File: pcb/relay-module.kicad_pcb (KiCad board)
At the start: 4 copper layers, 50 x 50 mm, 92 parts, among them J1 AVR-UPDI-6, J2 QWICC, J3 Power In, J4 Power Out, K1 PR24-5V-900-1A, P1 MountingHole_Pad, P2 MountingHole_Pad, P3 MountingHole_Pad, P4 MountingHole_Pad, Q1 MMBT3904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

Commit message: schematic and PCB clean up
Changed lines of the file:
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@@
 				(font
 					(size 0.001 0.001)
+					(thickness 0.15)
 				)
 			)
@@
 				(font
 					(size 0.001 0.001)
+					(thickness 0.15)
 				)
 			)
@@
 				(font
 					(size 0.001 0.001)
+					(thickness 0.15)
 				)
 				(justify mirror)
@@
 				(font
 					(size 0.001 0.001)
+					(thickness 0.15)
 				)
 				(justify mirror)
@@
 				(font
 					(size 0.001 0.001)
+					(thickness 0.15)
 				)
 				(justify mirror)
@@
 				(font
 					(size 0.001 0.001)
+					(thickness 0.15)
 				)
 				(justify mirror)
@@
 				(font
 					(size 0.001 0.001)
+					(thickness 0.15)
 				)
 				(justify mirror)
@@
 				(font
 					(size 0.001 0.001)
+					(thickness 0.15)
 				)
 				(justify mirror)
@@
 				(font
 					(size 0.001 0.001)
+					(thickness 0.15)
 				)
 				(justify mirror)
@@
 				(font
 					(size 0.001 0.001)
+					(thickness 0.15)
 				)
 				(justify mirror)
@@
 				(font
 					(size 0.001 0.001)
+					(thickness 0.15)
 				)
 				(justify mirror)
@@
 				(font
 					(size 0.001 0.001)
+					(thickness 0.15)
 				)
 				(justify mirror)
@@
 				(font
 					(size 0.001 0.001)
+					(thickness 0.15)
 				)
 				(justify mirror)
@@
 				(font
 					(size 0.001 0.001)
+					(thickness 0.15)
 				)
 				(justify mirror)
@@
 				(font
 					(size 0.001 0.001)
+					(thickness 0.15)
 				)
 				(justify mirror)
@@
 				(font
 					(size 0.001 0.001)
+					(thickness 0.15)
 				)
 				(justify mirror)
@@
 				(font
 					(size 0.001 0.001)
+					(thickness 0.15)
 				)
 				(justify mirror)
@@
 				(font
 					(size 0.001 0.001)
+					(thickness 0.15)
 				)
 				(justify mirror)
@@
 				(font
 					(size 0.001 0.001)
+					(thickness 0.15)
 				)
 				(justify mirror)
@@
 				(font
 					(size 0.001 0.001)
+					(thickness 0.15)
 				)
 				(justify mirror)
@@
 				(font
 					(size 0.001 0.001)
+					(thickness 0.15)
 				)
 				(justify mirror)
@@
 				(font
 					(size 0.001 0.001)
+					(thickness 0.15)
 				)
 				(justify mirror)
@@
 				(font
 					(size 0.001 0.001)
+					(thickness 0.15)
 				)
 				(justify mirror)
@@
 				(font
 					(size 0.001 0.001)
+					(thickness 0.15)
 				)
 				(justify mirror)
@@
 				(font
 					(size 0.001 0.001)
+					(thickness 0.15)
 				)
 				(justify mirror)
@@
 				(font
 					(size 0.001 0.001)
+					(thickness 0.15)
 				)
 				(justify mirror)
@@
 				(font
 					(size 0.001 0.001)
+					(thickness 0.15)
 				)
 				(justify mirror)
@@
 				(font
 					(size 0.001 0.001)
+					(thickness 0.15)
 				)
 				(justify mirror)
@@
 				(font
 					(size 0.001 0.001)
+					(thickness 0.15)
 				)
 				(justify mirror)
@@
 				(font
 					(size 0.001 0.001)
+					(thickness 0.15)
 				)
 				(justify mirror)
@@
 	)
 	(segment
-		(start 58.1 140.9)
-		(end 60.5 140.9)
+		(start 60.5 140.9)
+		(end 61.55 139.85)
 		(width 0.1524)
 		(layer "F.Cu")
@@
 	)
 	(segment
-		(start 57.4 140.2)
-		(end 58.1 140.9)
+		(start 57.7 140.15)
+		(end 58.45 140.9)
 		(width 0.1524)
 		(layer "F.Cu")
@@
 	)
 	(segment
-		(start 57.4 136.3)
-		(end 57.4 140.2)
+		(start 61.55 139.85)
+		(end 61.55 139.8)
 		(width 0.1524)
 		(layer "F.Cu")
@@
 	)
 	(segment
-		(start 54.45 133.35)
-		(end 57.4 136.3)
+		(start 54.45 133.2)
+		(end 54.45 133.35)
 		(width 0.1524)
 		(layer "F.Cu")
@@
 	)
 	(segment
-		(start 61.55 139.85)
-		(end 61.55 139.8)
+		(start 54.45 133.35)
+		(end 57.7 136.6)
 		(width 0.1524)
 		(layer "F.Cu")
@@
 	)
 	(segment
-		(start 60.5 140.9)
-		(end 61.55 139.85)
+		(start 57.7 136.6)
+		(end 57.7 140.15)
 		(width 0.1524)
 		(layer "F.Cu")
@@
 	)
 	(segment
-		(start 54.45 133.2)
-		(end 54.45 133.35)
+		(start 58.45 140.9)
+		(end 60.5 140.9)
 		(width 0.1524)
 		(layer "F.Cu")
@@
 	)
 	(segment
-		(start 58.25 140.35)
-		(end 59.95 140.35)
+		(start 59.95 140.35)
+		(end 60.9 139.4)
 		(width 0.1524)
 		(layer "F.Cu")
@@
 	)
 	(segment
-		(start 57.8 139.9)
-		(end 58.25 140.35)
+		(start 58.2 139.9)
+		(end 58.65 140.35)
 		(width 0.1524)
 		(layer "F.Cu")
@@
 	)
 	(segment
-		(start 56.55 134.25)
-		(end 57.8 135.5)
+		(start 60.9 139.4)
+		(end 61.55 139.4)
 		(width 0.1524)
 		(layer "F.Cu")
@@
 	)
 	(segment
-		(start 59.95 140.35)
-		(end 60.9 139.4)
+		(start 58.65 140.35)
+		(end 59.95 140.35)
 		(width 0.1524)
 		(layer "F.Cu")
@@
 	)
 	(segment
-		(start 57.8 135.5)
-		(end 57.8 139.9)
+		(start 56.55 134.25)
+		(end 58.2 135.9)
 		(width 0.1524)
 		(layer "F.Cu")
@@
 	)
 	(segment
-		(start 60.9 139.4)
-		(end 61.55 139.4)
+		(start 58.2 135.9)
+		(end 58.2 139.9)
 		(width 0.1524)
 		(layer "F.Cu")

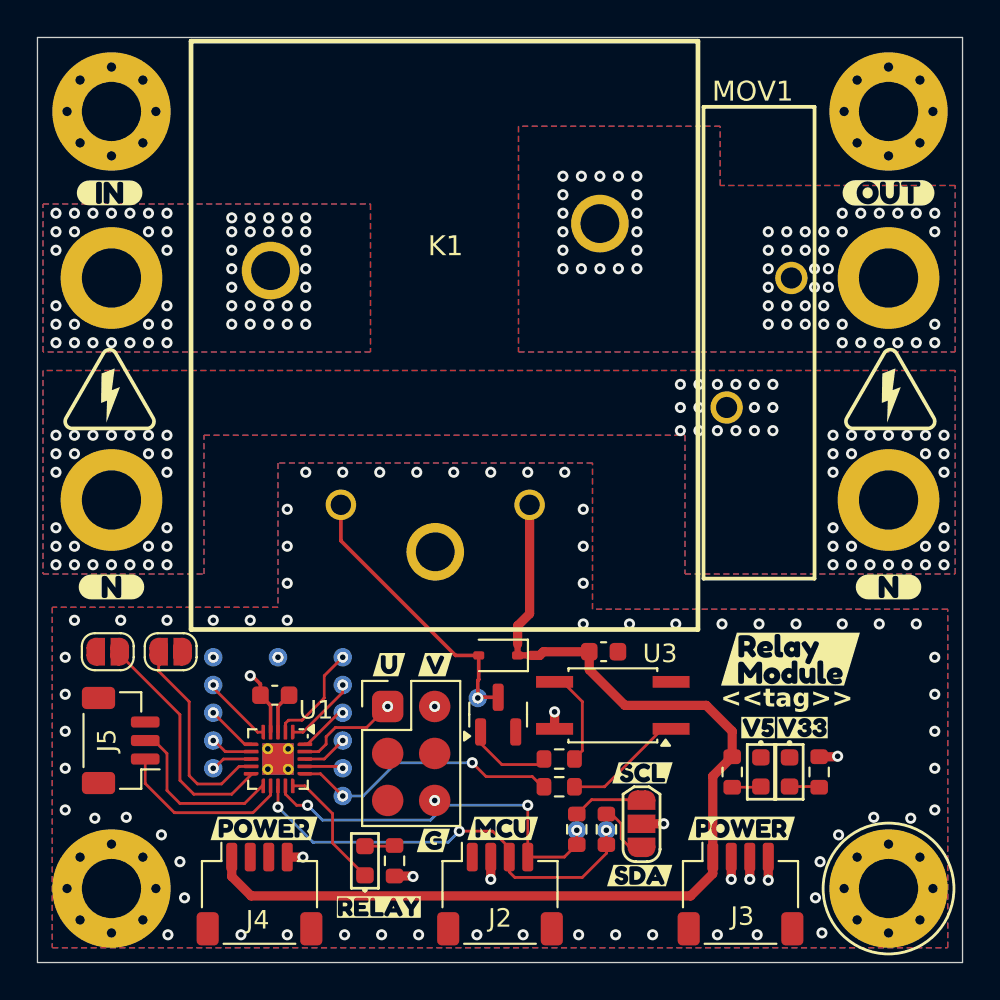
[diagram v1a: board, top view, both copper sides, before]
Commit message: Updated mounting holes; rounded corners
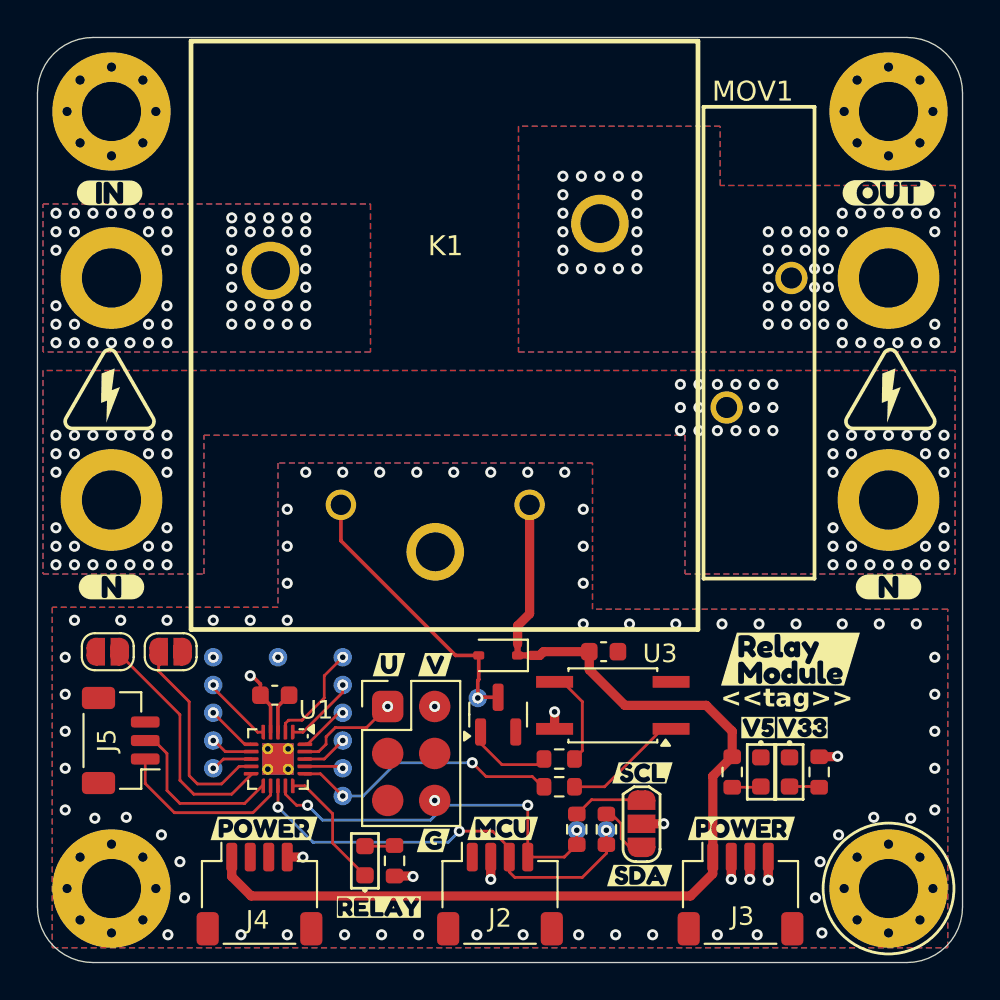
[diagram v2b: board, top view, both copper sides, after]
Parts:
- P1, P2, P3, P4: footprint MountingHole:MountingHole_3.2mm_M3_ISO14580_Pad -> CRGM Mechanical:MountingHole_3.2mm_M3_ISO14580_Pad
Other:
- outline, holes or cut-outs redrawn
- board text added: "x 8"

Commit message: Changed to multi-sheet
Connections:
- net /A0 renamed /MCU/A0
- net /A1 renamed /MCU/A1
- net /LOAD_IN renamed /Relay/LOAD_IN
- net /LOAD_OUT renamed /Relay/LOAD_OUT
- net /NEUTRAL renamed /Relay/NEUTRAL
- net /PA1 renamed /MCU/PA1
- net /PA2 renamed /MCU/PA2
- net /PA3 renamed /MCU/PA3
- net /PA4 renamed /MCU/PA4
- net /PA5 renamed /MCU/PA5
- net /PA6 renamed /MCU/PA6
- net /PA7 renamed /MCU/PA7
- net /PC2 renamed /MCU/PC2
- net /PC3 renamed /MCU/PC3
- net /RELAY_CTRL renamed /Relay/RELAY_CTRL
- net /SCL renamed SCL
- net /SDA renamed SDA
- net /V3.3LED renamed /MCU/V3.3LED
- net /V5LED renamed /MCU/V5LED
